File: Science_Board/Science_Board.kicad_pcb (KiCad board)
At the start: 2 copper layers, 108.3 x 85.5 mm, 145 parts, among them IC1 TCKE603RA, IC2 TCKE603RA, IC3 TCKE603RM, J1 Conn_01x02, J10 Conn_01x02, J11 Conn_01x03, J12 Conn_01x03, J13 Conn_01x03, J14 Conn_01x03, J15 Conn_01x03, J16 Conn_01x03, J17 Conn_01x03, J18 Conn_01x03, J19 Conn_01x02, J2 RJ45_LED_Shielded, J20 Molex_Megafit_02, J21 Molex_Megafit_02, J22 Molex_Megafit_02, J23 Conn_01x02, J24 Conn_01x02, J3 Molex_Megafit_02, J4 Molex_Megafit_02, J5 Conn_01x05, J6 Conn_01x04, J7 Conn_01x03, J8 Conn_01x03, J9 Conn_01x02, Q1 BS250, Q2 NMOS, Q3 NMOS, Q4 NMOS, Q5 NMOS, Q6 NMOS, SW1 SW_Push, SW10 SW_Push, SW11 SW_Push, SW12 SW_SPDT, SW2 SW_Push, SW3 SW_Push, SW4 SW_Push, SW5 SW_Push, SW6 SW_Push, SW7 SW_Push, SW8 SW_Push, SW9 SW_Push, U3 LM22678TJ-5, U5 PCA9685PW

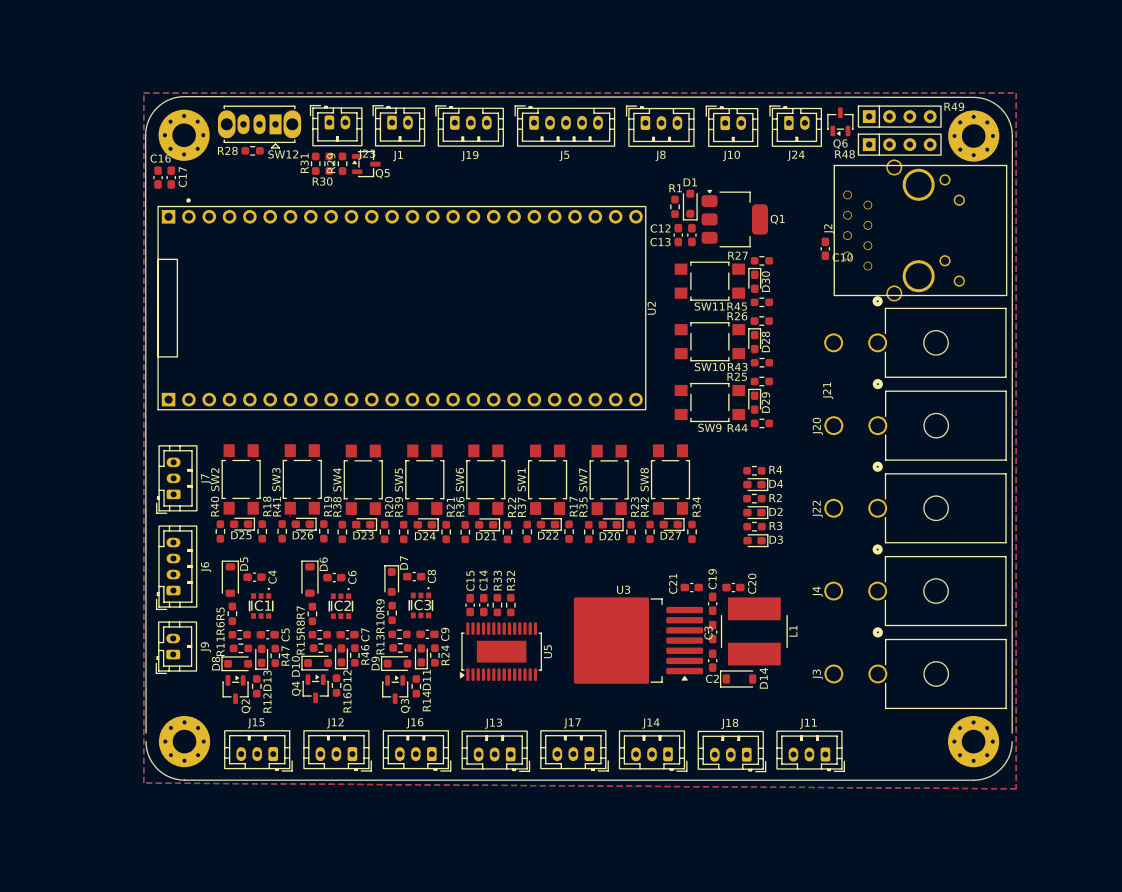
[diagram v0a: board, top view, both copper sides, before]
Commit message: more space save on layout
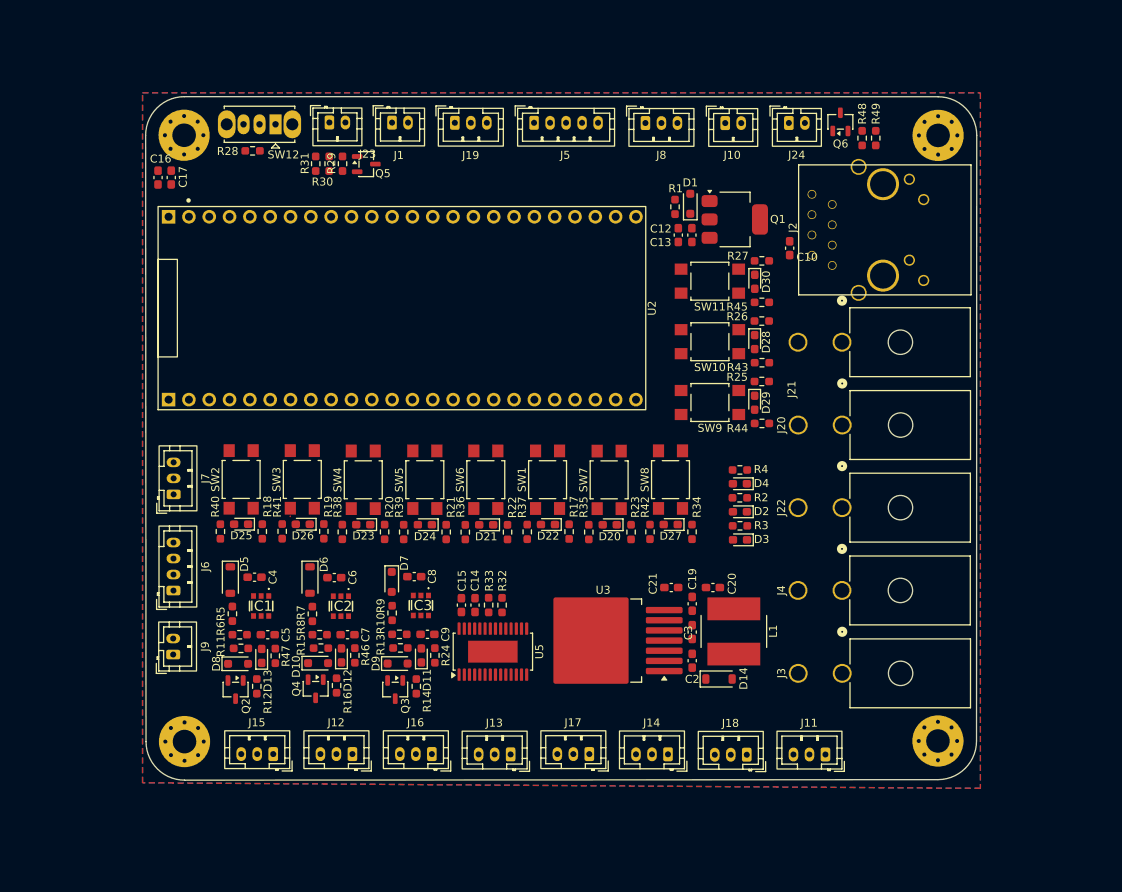
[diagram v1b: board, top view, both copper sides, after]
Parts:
- R48, R49: footprint Resistor_THT:R_Array_SIP4 -> Resistor_SMD:R_0603_1608Metric_Pad0.98x0.95mm_HandSolder
- moved H3 4.45 mm to (182.1, 142.6)
- moved H4 4.45 mm to (182.1, 66.9)
- moved J2 4.45 mm to (188.2, 78.6)
- moved J20 4.45 mm to (170.1, 103.1)
- moved J21 4.45 mm to (170.1, 92.8)
- moved J22 4.45 mm to (170.1, 113.5)
- moved J3 4.45 mm to (170.1, 134.2)
- moved J4 4.45 mm to (170.1, 123.8)
- moved C10 4.45 mm to (163.5, 81.0)
- moved R49 2.81 mm to (174.3, 67.3), turned to -90 degrees
- moved C21 2.56 mm to (148.7, 123.4)
- moved U3 2.56 mm to (140.2, 130.1)
- moved C19 2.56 mm to (151.4, 125.5)
- moved C2 2.56 mm to (151.4, 132.6)
- moved C20 2.56 mm to (153.9, 123.4)
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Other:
- board size 108.3 x 85.5 mm -> 103.9 x 85.4 mm

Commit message: changed some text
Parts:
- moved J9 0.79 mm to (86.4, 132.6)
- moved J6 0.79 mm to (86.5, 124.6)
- moved J7 0.79 mm to (86.5, 112.6)
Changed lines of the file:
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@@
 		(tags "CMS SOT")
 		(property "Reference" "Q1"
-			(at 5.3848 -0.0254 0)
+			(at -0.03598 -4.333807 0)
 			(layer "F.SilkS")
 			(effects
@@
 		(tags "SOD-123")
 		(property "Reference" "D14"
-			(at 3.0744 -0.0519 90)
+			(at 3.7902 -0.0201 0)
 			(layer "F.SilkS")
 			(effects
@@
 		(tags "capacitor handsolder")
 		(property "Reference" "C13"
-			(at -0.9155 -3.9116 0)
+			(at -2.358 1.5426 0)
 			(layer "F.SilkS")
 			(effects
@@
 	(footprint "Connector_JST:JST_PH_B4B-PH-K_1x04_P2.00mm_Vertical"
 		(layer "F.Cu")
-		(at 86.5124 123.8118 90)
+		(at 86.4792 124.5992 90)
 		(descr "JST PH series connector, B4B-PH-K (http://www.jst-mfg.com/product/pdf/eng/ePH.pdf)")
 		(tags "connector JST PH vertical")
@@
 		(tags "capacitor handsolder")
 		(property "Reference" "C20"
-			(at 2.3887 -0.4837 90)
+			(at 3.0791 0.0561 180)
 			(layer "F.SilkS")
 			(effects
@@
 	(footprint "Connector_JST:JST_PH_B2B-PH-K_1x02_P2.00mm_Vertical"
 		(layer "F.Cu")
-		(at 86.4782 131.81 90)
+		(at 86.445 132.5974 90)
 		(descr "JST PH series connector, B2B-PH-K (http://www.jst-mfg.com/product/pdf/eng/ePH.pdf)")
 		(tags "connector JST PH vertical")
@@
 		(tags "capacitor handsolder")
 		(property "Reference" "C19"
-			(at -3.0999 -0.0254 90)
+			(at -3.3729 -0.0046 180)
 			(layer "F.SilkS")
 			(effects
@@
 		(tags "capacitor handsolder")
 		(property "Reference" "C12"
-			(at -0.7874 2.1844 0)
+			(at 2.3569 -0.5266 0)
 			(layer "F.SilkS")
 			(effects
@@
 	(footprint "Connector_JST:JST_PH_B3B-PH-K_1x03_P2.00mm_Vertical"
 		(layer "F.Cu")
-		(at 86.529 111.7882 90)
+		(at 86.4958 112.5756 90)
 		(descr "JST PH series connector, B3B-PH-K (http://www.jst-mfg.com/product/pdf/eng/ePH.pdf)")
 		(tags "connector JST PH vertical")
@@
 		(tags "capacitor handsolder")
 		(property "Reference" "C21"
-			(at 2.286 0.4826 90)
+			(at 3.0434 -0.0318 180)
 			(layer "F.SilkS")
 			(effects
@@
 		(tags "HTSSOP SO")
 		(property "Reference" "U5"
-			(at 0 5.8199 90)
+			(at 4.6276 3.2799 180)
 			(layer "F.SilkS")
 			(effects
@@
 		(tags "768250002 ")
 		(property "Reference" "J21"
-			(at -5.8928 -6.2825 90)
+			(at 0.060528 -7.5946 90)
 			(unlocked yes)
 			(layer "F.SilkS")
@@
 		(tags "Inductor")
 		(property "Reference" "L1"
-			(at 0.0264 4.9182 90)
+			(at 5.3795 3.4855 180)
 			(layer "F.SilkS")
 			(effects

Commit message: reorganized
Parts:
- moved D29 24.1 mm to (159.1, 76.2)
- moved R44 24.1 mm to (160.0, 78.8)
- moved SW9 24.1 mm to (153.5, 76.2)
- moved R25 24.1 mm to (160.0, 73.6)
- moved C12 22.6 mm to (150.1, 102.0)
- moved C13 22.6 mm to (151.8, 102.0)
- moved D1 22.6 mm to (151.6, 98.1)
- moved Q1 22.6 mm to (157.1, 100.0)
- moved R1 22.6 mm to (149.7, 98.5)
- moved J22 20.7 mm to (170.1, 134.2)
- moved J4 10.3 mm to (170.1, 113.5)
- moved J3 10.3 mm to (170.1, 123.8)
- moved D30 1.37 mm to (159.1, 83.8)
- moved R26 1.37 mm to (160.0, 88.8)
- moved R43 1.37 mm to (160.0, 94.0)
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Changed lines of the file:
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@@
 	(footprint "Package_TO_SOT_SMD:SOT-223"
 		(layer "F.Cu")
-		(at 156.674 77.4245)
+		(at 157.147729 100.027459)
 		(descr "module CMS SOT223 4 pins")
 		(tags "CMS SOT")
@@
 	(footprint "Capacitor_SMD:C_0603_1608Metric_Pad1.08x0.95mm_HandSolder"
 		(layer "F.Cu")
-		(at 151.3146 79.3792 90)
+		(at 151.788329 101.982159 90)
 		(descr "Capacitor SMD 0603 (1608 Metric), square (rectangular) end terminal, IPC-7351 nominal with elongated pad for handsoldering. (Body size source: IPC-SM-782 page 76, https://www.pcb-3d.com/wordpress/wp-content/uploads/ipc-sm-782a_amendment_1_and_2.pdf)")
 		(tags "capacitor handsolder")
@@
 	(footprint "Button_Switch_SMD:SW_SPST_TL3305A"
 		(layer "F.Cu")
-		(at 153.5684 92.71 180)
+		(at 153.5244 91.337 180)
 		(descr "https://www.e-switch.com/system/asset/product_line/data_sheet/213/TL3305.pdf")
 		(tags "TL3305 Series Tact Switch")
@@
 	(footprint "Resistor_SMD:R_0603_1608Metric_Pad0.98x0.95mm_HandSolder"
 		(layer "F.Cu")
-		(at 160.0541 97.6784 180)
+		(at 159.9525 73.5682 180)
 		(descr "Resistor SMD 0603 (1608 Metric), square (rectangular) end terminal, IPC-7351 nominal with elongated pad for handsoldering. (Body size source: IPC-SM-782 page 72, https://www.pcb-3d.com/wordpress/wp-content/uploads/ipc-sm-782a_amendment_1_and_2.pdf)")
 		(tags "resistor handsolder")
@@
 	(footprint "LED_SMD:LED_0603_1608Metric_Pad1.05x0.95mm_HandSolder"
 		(layer "F.Cu")
-		(at 159.1613 100.3314 -90)
+		(at 159.0597 76.2212 -90)
 		(descr "LED SMD 0603 (1608 Metric), square (rectangular) end terminal, IPC-7351 nominal, (Body size source: http://www.tortai-tech.com/upload/download/2011102023233369053.pdf)")
 		(tags "LED handsolder")
@@
 	(footprint "Diode_SMD:D_SOD-323_HandSoldering"
 		(layer "F.Cu")
-		(at 151.1114 75.46435 90)
+		(at 151.585129 98.067309 90)
 		(descr "SOD-323")
 		(tags "SOD-323")
 		(property "Reference" "D1"
-			(at 2.63725 0 0)
+			(at 2.309309 1.856271 0)
 			(layer "F.SilkS")
 			(effects
@@
 	(footprint "Resistor_SMD:R_0603_1608Metric_Pad0.98x0.95mm_HandSolder"
 		(layer "F.Cu")
-		(at 149.2064 75.849341 90)
+		(at 149.680129 98.4523 90)
 		(descr "Resistor SMD 0603 (1608 Metric), square (rectangular) end terminal, IPC-7351 nominal with elongated pad for handsoldering. (Body size source: IPC-SM-782 page 72, https://www.pcb-3d.com/wordpress/wp-content/uploads/ipc-sm-782a_amendment_1_and_2.pdf)")
 		(tags "resistor handsolder")
@@
 	(footprint "MRDT_Connectors:MOLEX_MegaFit_02_Horizontal"
 		(layer "F.Cu")
-		(at 170.0784 123.798387 90)
+		(at 170.062249 113.4618 90)
 		(tags "768250002 ")
 		(property "Reference" "J4"
@@
 	(footprint "Button_Switch_SMD:SW_SPST_TL3305A"
 		(layer "F.Cu")
-		(at 153.5684 100.3074 180)
+		(at 153.4668 76.1972 180)
 		(descr "https://www.e-switch.com/system/asset/product_line/data_sheet/213/TL3305.pdf")
 		(tags "TL3305 Series Tact Switch")
@@
 	(footprint "Button_Switch_SMD:SW_SPST_TL3305A"
 		(layer "F.Cu")
-		(at 153.5597 85.1436 180)
+		(at 153.5157 83.7706 180)
 		(descr "https://www.e-switch.com/system/asset/product_line/data_sheet/213/TL3305.pdf")
 		(tags "TL3305 Series Tact Switch")
@@
 	(footprint "Capacitor_SMD:C_0603_1608Metric_Pad1.08x0.95mm_HandSolder"
 		(layer "F.Cu")
-		(at 149.6128 79.3803 -90)
+		(at 150.086529 101.983259 -90)
 		(descr "Capacitor SMD 0603 (1608 Metric), square (rectangular) end terminal, IPC-7351 nominal with elongated pad for handsoldering. (Body size source: IPC-SM-782 page 76, https://www.pcb-3d.com/wordpress/wp-content/uploads/ipc-sm-782a_amendment_1_and_2.pdf)")
 		(tags "capacitor handsolder")
@@
 	(footprint "LED_SMD:LED_0603_1608Metric_Pad1.05x0.95mm_HandSolder"
 		(layer "F.Cu")
-		(at 159.1632 92.7556 -90)
+		(at 159.1192 91.3826 -90)
 		(descr "LED SMD 0603 (1608 Metric), square (rectangular) end terminal, IPC-7351 nominal, (Body size source: http://www.tortai-tech.com/upload/download/2011102023233369053.pdf)")
 		(tags "LED handsolder")
@@
 	(footprint "Resistor_SMD:R_0603_1608Metric_Pad0.98x0.95mm_HandSolder"
 		(layer "F.Cu")
-		(at 160.0621 82.6036 180)
+		(at 160.0181 81.2306 180)
 		(descr "Resistor SMD 0603 (1608 Metric), square (rectangular) end terminal, IPC-7351 nominal with elongated pad for handsoldering. (Body size source: IPC-SM-782 page 72, https://www.pcb-3d.com/wordpress/wp-content/uploads/ipc-sm-782a_amendment_1_and_2.pdf)")
 		(tags "resistor handsolder")
@@
 	(footprint "Resistor_SMD:R_0603_1608Metric_Pad0.98x0.95mm_HandSolder"
 		(layer "F.Cu")
-		(at 160.0522 90.1254 180)
+		(at 160.0082 88.7524 180)
 		(descr "Resistor SMD 0603 (1608 Metric), square (rectangular) end terminal, IPC-7351 nominal with elongated pad for handsoldering. (Body size source: IPC-SM-782 page 72, https://www.pcb-3d.com/wordpress/wp-content/uploads/ipc-sm-782a_amendment_1_and_2.pdf)")
 		(tags "resistor handsolder")
@@
 	(footprint "MRDT_Connectors:MOLEX_MegaFit_02_Horizontal"
 		(layer "F.Cu")
-		(at 170.1038 134.161587 90)
+		(at 170.087649 123.825 90)
 		(tags "768250002 ")
 		(property "Reference" "J3"
@@
 	(footprint "Resistor_SMD:R_0603_1608Metric_Pad0.98x0.95mm_HandSolder"
 		(layer "F.Cu")
-		(at 160.0757 95.3324 180)
+		(at 160.0317 93.9594 180)
 		(descr "Resistor SMD 0603 (1608 Metric), square (rectangular) end terminal, IPC-7351 nominal with elongated pad for handsoldering. (Body size source: IPC-SM-782 page 72, https://www.pcb-3d.com/wordpress/wp-content/uploads/ipc-sm-782a_amendment_1_and_2.pdf)")
 		(tags "resistor handsolder")
@@
 	(footprint "Resistor_SMD:R_0603_1608Metric_Pad0.98x0.95mm_HandSolder"
 		(layer "F.Cu")
-		(at 160.0738 102.9222 180)
+		(at 159.9722 78.812 180)
 		(descr "Resistor SMD 0603 (1608 Metric), square (rectangular) end terminal, IPC-7351 nominal with elongated pad for handsoldering. (Body size source: IPC-SM-782 page 72, https://www.pcb-3d.com/wordpress/wp-content/uploads/ipc-sm-782a_amendment_1_and_2.pdf)")
 		(tags "resistor handsolder")
@@
 	(footprint "MRDT_Connectors:MOLEX_MegaFit_02_Horizontal"
 		(layer "F.Cu")
-		(at 170.087649 113.450859 90)
+		(at 170.1038 134.161587 90)
 		(tags "768250002 ")
 		(property "Reference" "J22"
@@
 	(footprint "Resistor_SMD:R_0603_1608Metric_Pad0.98x0.95mm_HandSolder"
 		(layer "F.Cu")
-		(at 160.0621 87.7852 180)
+		(at 160.0181 86.4122 180)
 		(descr "Resistor SMD 0603 (1608 Metric), square (rectangular) end terminal, IPC-7351 nominal with elongated pad for handsoldering. (Body size source: IPC-SM-782 page 72, https://www.pcb-3d.com/wordpress/wp-content/uploads/ipc-sm-782a_amendment_1_and_2.pdf)")
 		(tags "resistor handsolder")
@@
 	(footprint "LED_SMD:LED_0603_1608Metric_Pad1.05x0.95mm_HandSolder"
 		(layer "F.Cu")
-		(at 159.1731 85.2198 -90)
+		(at 159.1291 83.8468 -90)
 		(descr "LED SMD 0603 (1608 Metric), square (rectangular) end terminal, IPC-7351 nominal, (Body size source: http://www.tortai-tech.com/upload/download/2011102023233369053.pdf)")
 		(tags "LED handsolder")

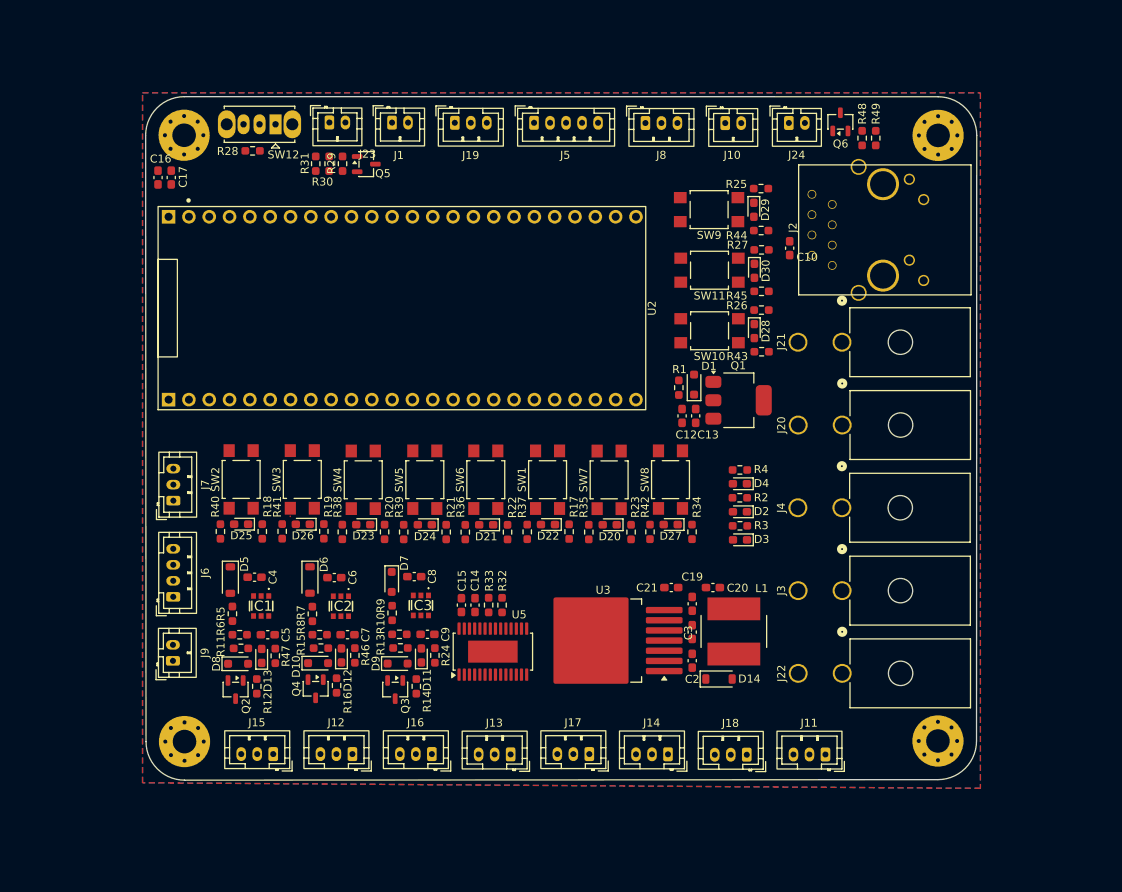
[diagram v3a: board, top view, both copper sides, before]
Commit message: Diode now has the correct footprint and made the mounting holes the correct distance apart
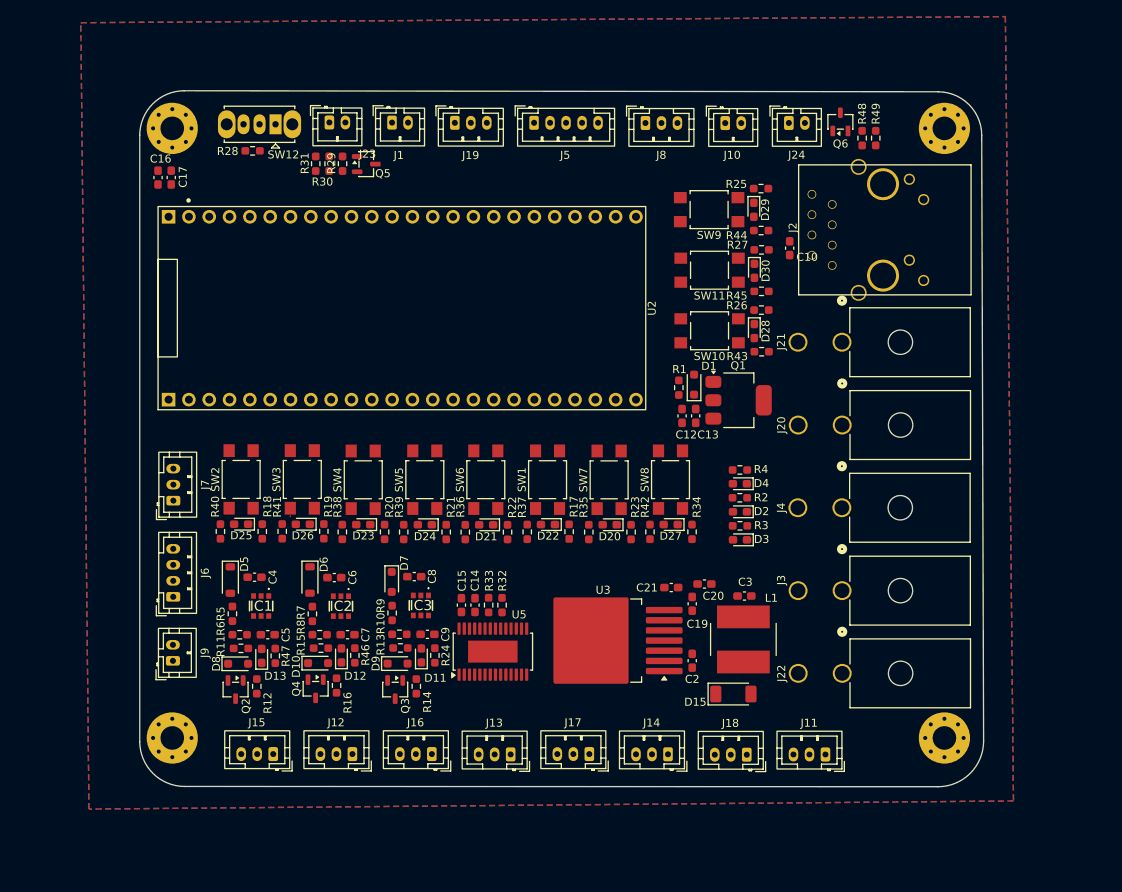
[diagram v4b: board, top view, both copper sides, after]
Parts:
- removed D14: 28V, Diode_SMD:D_SOD-123
- added D15: D_Schottky, Diode_SMD:D_SOD-128, F.Cu at (156.5, 136.8)
- moved C3 7.93 mm to (157.9, 124.5), turned to 180 degrees
- moved H2 1.71 mm to (86.4, 66.0)
- moved H1 1.60 mm to (86.4, 142.2)
- moved L1 1.55 mm to (157.8, 129.9)
- moved H4 1.18 mm to (182.9, 66.0)
- moved C20 1.14 mm to (152.9, 123.0)
- moved H3 0.89 mm to (182.9, 142.2)
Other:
- board size 103.9 x 85.4 mm -> 105.5 x 87 mm

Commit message: crisp dimensions
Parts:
- moved C12 1.08 mm to (149.1, 102.4)
- moved C13 1.08 mm to (150.8, 102.4)
- moved C14 1.08 mm to (123.2, 126.1)
- moved C19 1.08 mm to (150.4, 125.9)
- moved C2 1.08 mm to (150.4, 133.0)
- moved C21 1.08 mm to (147.8, 123.9)
- moved C4 1.08 mm to (95.7, 122.6)
- moved C5 1.08 mm to (97.3, 129.8)
- moved C6 1.08 mm to (105.6, 122.7)
- moved C8 1.08 mm to (115.6, 122.5)
- moved D1 1.08 mm to (150.6, 98.5)
- moved D10 1.08 mm to (103.6, 133.3)
- moved D13 1.08 mm to (96.6, 132.4)
- moved D15 1.08 mm to (155.5, 137.2)
- moved D2 1.08 mm to (156.3, 114.4)
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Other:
- board size 105.5 x 87 mm -> 106.8 x 87.8 mm
